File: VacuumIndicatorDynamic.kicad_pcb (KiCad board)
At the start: 2 copper layers, 96 parts, among them J1 Conn_01x02_Male, J2 Conn_01x03_Male, J3 Conn_01x03_Male, J4 Conn_01x03_Male, SW1 SW_DIP_x01, SW2 SW_DIP_x01, SW3 SW_DIP_x01, SW4 SW_DIP_x01, U1 AP1117-25, U2 YAAJ_BluePill

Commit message: update pcb
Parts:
- added REF**: KiCad-Logo2_8mm_Copper, Symbol:KiCad-Logo2_8mm_Copper, F.Cu at (85.7, 109.9)
- J1: moved to B.Cu
- moved R38 35.0 mm to (184.8, 34.3)
- moved R42 35.0 mm to (184.8, 40.4)
- moved R46 35.0 mm to (175.5, 36.2)
- moved VT22 35.0 mm to (179.8, 36.2)
- moved R50 35.0 mm to (175.9, 40.6)
- moved VT26 35.0 mm to (180.9, 39.4)
- moved R21 24.4 mm to (160.8, 117.0), turned to 180 degrees
- moved VT15 20.3 mm to (161.9, 113.7), turned to 180 degrees
- moved R31 20.2 mm to (160.0, 108.7), turned to 90 degrees
- moved R16 18.8 mm to (166.5, 117.0), turned to 180 degrees
- moved VT10 15.7 mm to (165.1, 112.5), turned to 0 degrees
- moved R26 13.2 mm to (165.1, 108.7), turned to 90 degrees
- moved R34 11.4 mm to (176.5, 90.8)
- moved VT24 11.4 mm to (181.4, 64.1)
- moved R18 11.4 mm to (184.9, 97.2)
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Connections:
- U2 pad 11: /AU3 -> /AU9
- U2 pad 12: /AU4 -> /AU8
- U2 pad 13: /AU5 -> /AU7
- U2 pad 15: /AU7 -> /AU5
- U2 pad 16: /AU8 -> /AU4
- U2 pad 17: /AU9 -> /AU3
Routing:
- net +2V5: track 215.3 -> 184.3 mm, vias 1 -> 2
- net /A3: track 19.1 -> 32.7 mm
- net /A6: track 31.2 -> 19.4 mm
- net /A7: track 38.4 -> 26.6 mm
- net +24V: track 234.6 -> 223.4 mm
- net /A2: track 28.5 -> 38.6 mm
- net /A4: track 14.0 -> 22.9 mm
- net GND: track 670.9 -> 662.2 mm, vias 11 -> 13
- net Net-(R38-Pad2): track 0.00 -> 8.06 mm
- net /A5: track 21.6 -> 14.2 mm
- net +3V3: track 123.7 -> 130.6 mm
- net /A1: track 36.3 -> 29.9 mm
- net Net-(R42-Pad2): track 0.00 -> 4.19 mm
- net /A8: track 30.0 -> 33.5 mm
- net +5V: track 245.0 -> 248.4 mm
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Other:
- board text added: "Dolgopolov"

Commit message: update pcb
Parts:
- moved J4 1.90 mm to (183.5, 28.6)
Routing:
- net GND: track 662.2 -> 695.5 mm
- net +24V: track 223.4 -> 228.7 mm
- net /A9: track 47.5 -> 50.5 mm
- net /AU8: track 44.5 -> 47.1 mm, vias 1 -> 2
- net /AU1: track 102.9 -> 100.4 mm
- net Net-(EL1-Pad12): track 144.2 -> 146.4 mm
- net /A7: track 26.6 -> 24.6 mm
- net Net-(EL1-Pad13): track 137.0 -> 139.0 mm
- net +2V5: track 184.3 -> 186.2 mm
- net /BTN1: track 97.5 -> 95.8 mm
- net /BTN2: track 83.3 -> 81.7 mm
- net Net-(EL1-Pad14): track 129.2 -> 130.8 mm
- net +3V3: track 130.6 -> 129.0 mm
- net /N: track 97.6 -> 96.2 mm
- net /AU2: track 100.1 -> 98.8 mm
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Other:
- board outline added: 167.2 x 100.6 mm

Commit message: pcb update. ready for fabrication
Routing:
- added copper zone on F.Cu, net GND
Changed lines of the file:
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@@
   (arc (start 41.783 57.277) (mid 41.783 57.277) (end 41.783 57.277) (width 0.4) (layer "F.Cu") (net 102))
   (segment (start 177.5575 99.06) (end 180.455 99.06) (width 0.8) (layer "F.Cu") (net 104))
+  (zone (net 2) (net_name "GND") (layer "F.Cu") (hatch edge 0.508)
+    (priority 1)
+    (connect_pads (clearance 1))
+    (min_thickness 0.254) (filled_areas_thickness no)
+    (fill yes (mode hatch) (thermal_gap 0.508) (thermal_bridge_width 0.508)
+      (hatch_thickness 1.016) (hatch_gap 1.524) (hatch_orientation 45)
+      (hatch_border_algorithm hatch_thickness) (hatch_min_hole_area 0.3))
+    (polygon
+      (pts
+        (xy 193 124)
+        (xy 123 124)
+        (xy 123 24)
+        (xy 193 24)
+      )
+    )
+  )
+  (zone (net 2) (net_name "GND") (layer "F.Cu") (hatch edge 0.508)
+    (priority 1)
+    (connect_pads (clearance 1))
+    (min_thickness 0.254) (filled_areas_thickness no)
+    (fill yes (mode hatch) (thermal_gap 0.508) (thermal_bridge_width 0.508)
+      (hatch_thickness 1.016) (hatch_gap 1.524) (hatch_orientation 45)
+      (hatch_border_algorithm hatch_thickness) (hatch_min_hole_area 0.3))
+    (polygon
+      (pts
+        (xy 96 124)
+        (xy 26 124)
+        (xy 26 23)
+        (xy 96 23)
+      )
+    )
+  )
 )

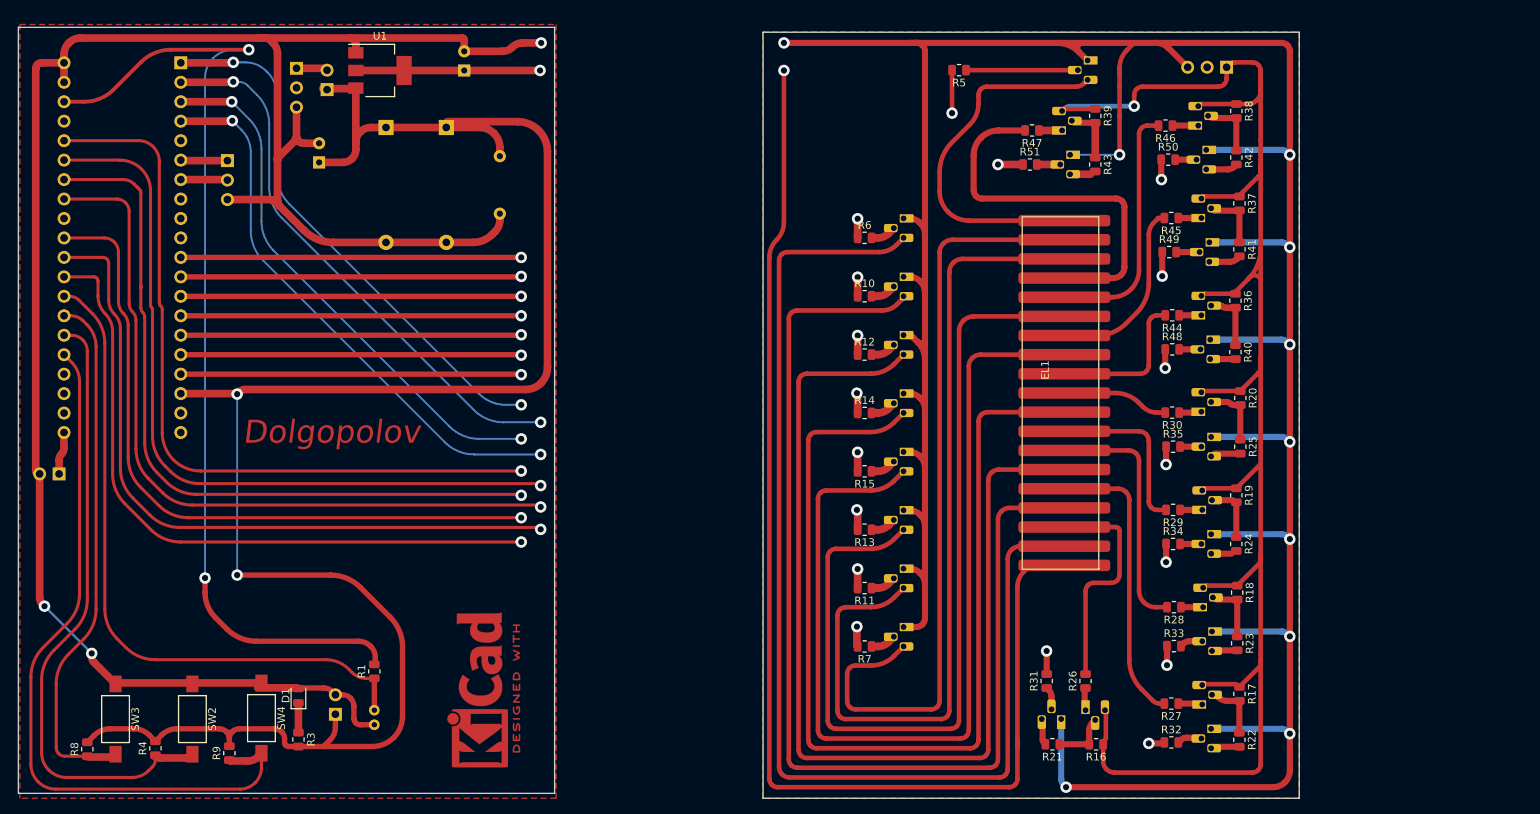
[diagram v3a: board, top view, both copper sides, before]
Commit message: remove copper area add mounting holes
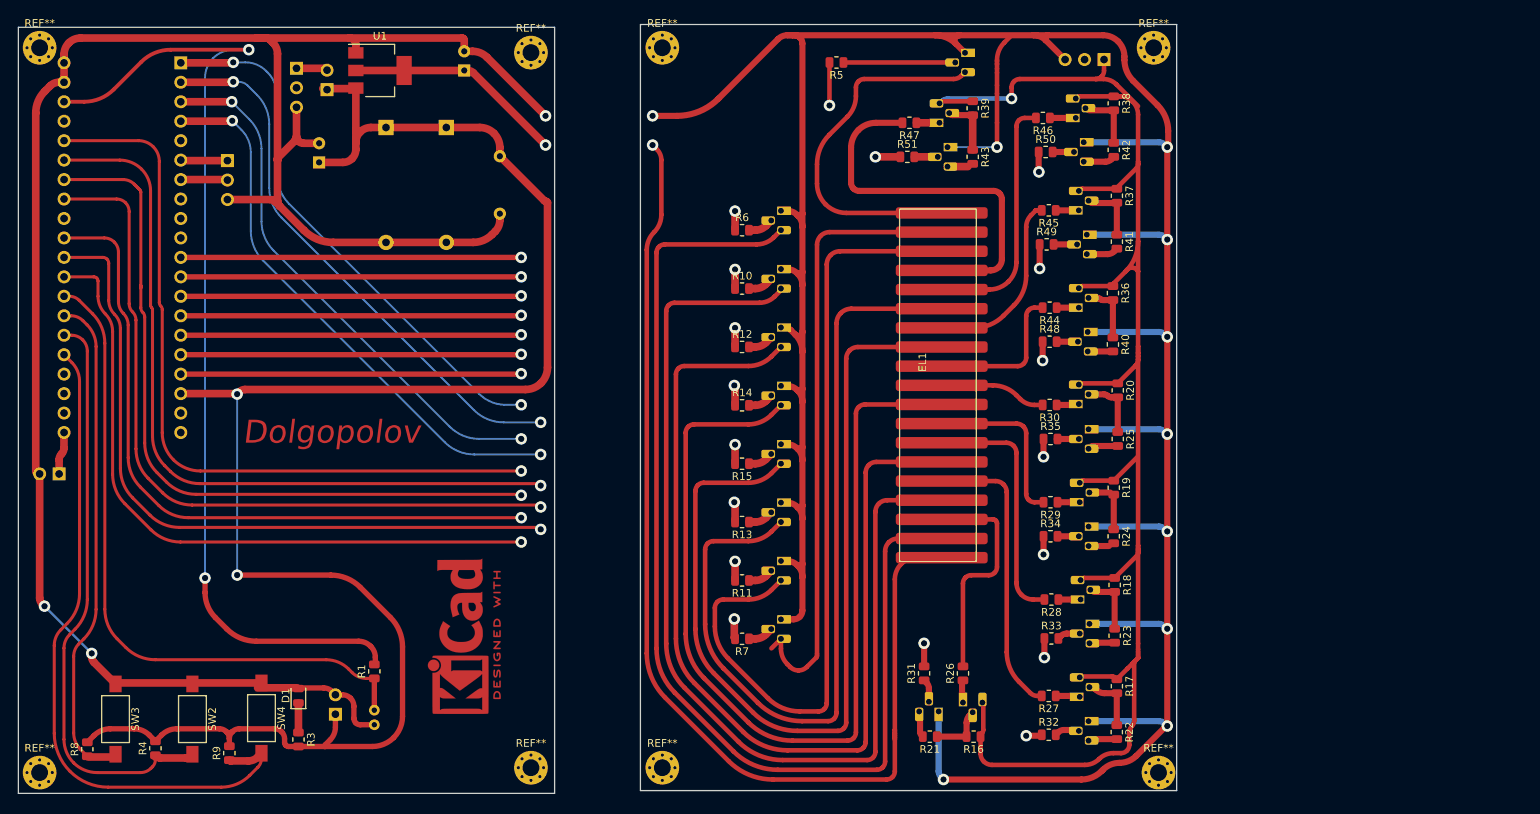
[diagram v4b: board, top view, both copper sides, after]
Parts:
- added REF**: MountingHole_2.2mm_M2_Pad_Via, MountingHole:MountingHole_2.2mm_M2_Pad_Via, F.Cu at (28.6, 26.0)
- added REF**: MountingHole_2.2mm_M2_Pad_Via, MountingHole:MountingHole_2.2mm_M2_Pad_Via, F.Cu at (174.6, 120.7)
- added REF**: MountingHole_2.2mm_M2_Pad_Via, MountingHole:MountingHole_2.2mm_M2_Pad_Via, F.Cu at (174.0, 26.0)
- added REF**: MountingHole_2.2mm_M2_Pad_Via, MountingHole:MountingHole_2.2mm_M2_Pad_Via, F.Cu at (109.9, 26.0)
- added REF**: MountingHole_2.2mm_M2_Pad_Via, MountingHole:MountingHole_2.2mm_M2_Pad_Via, F.Cu at (92.7, 120.0)
- added REF**: MountingHole_2.2mm_M2_Pad_Via, MountingHole:MountingHole_2.2mm_M2_Pad_Via, F.Cu at (109.9, 120.0)
- added REF**: MountingHole_2.2mm_M2_Pad_Via, MountingHole:MountingHole_2.2mm_M2_Pad_Via, F.Cu at (92.7, 26.7)
- added REF**: MountingHole_2.2mm_M2_Pad_Via, MountingHole:MountingHole_2.2mm_M2_Pad_Via, F.Cu at (28.6, 120.7)
- moved R10 16.0 mm to (120.3, 57.5)
- moved R11 16.0 mm to (120.3, 95.6)
- moved R12 16.0 mm to (120.3, 65.1)
- moved R13 16.0 mm to (120.3, 87.9)
- moved R14 16.0 mm to (120.3, 72.7)
- moved R15 16.0 mm to (120.3, 80.3)
- moved R6 16.0 mm to (120.3, 49.8)
- moved R7 16.0 mm to (120.3, 103.2)
- moved EL1 16.0 mm to (147.8, 70.1)
- moved J4 16.0 mm to (167.5, 27.6)
- moved R16 16.0 mm to (150.5, 116.0)
- moved R17 16.0 mm to (169.2, 109.4)
- moved R18 16.0 mm to (168.9, 96.2)
- moved R19 16.0 mm to (168.8, 83.5)
- moved R20 16.0 mm to (169.3, 70.8)
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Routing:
- net Net-(EL1-Pad19): track 101.4 -> 81.1 mm
- net +2V5: track 186.2 -> 172.8 mm
- net +5V: track 248.2 -> 235.0 mm
- net +24V: track 228.7 -> 219.4 mm
- net Net-(EL1-Pad12): track 146.4 -> 138.9 mm
- net Net-(EL1-Pad13): track 139.0 -> 131.8 mm
- net /BTN1: track 95.8 -> 88.9 mm
- net Net-(EL1-Pad14): track 130.8 -> 123.9 mm
- net Net-(EL1-Pad15): track 125.7 -> 119.2 mm
- net Net-(EL1-Pad16): track 124.5 -> 118.4 mm
- net Net-(EL1-Pad17): track 116.7 -> 110.9 mm
- net Net-(EL1-Pad18): track 112.1 -> 106.9 mm
- net /BTN2: track 81.7 -> 77.0 mm
- net /BTN3: track 68.9 -> 65.1 mm
- net GND: track 695.5 -> 692.5 mm
- removed copper zone on F.Cu, net GND
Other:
- board size 167.2 x 100.6 mm -> 151.2 x 100.4 mm

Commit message: several pcb updates
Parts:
- removed the REF** at (92.7, 120.0)
- removed the REF** at (109.9, 120.0)
- added REF**: MountingHole_2.2mm_M2_Pad_Via, MountingHole:MountingHole_2.2mm_M2_Pad_Via, F.Cu at (92.7, 120.7)
- added REF**: MountingHole_2.2mm_M2_Pad_Via, MountingHole:MountingHole_2.2mm_M2_Pad_Via, F.Cu at (109.9, 120.7)
- C3: footprint Capacitor_THT:C_Axial_L5.1mm_D3.1mm_P7.50mm_Horizontal -> Capacitor_SMD:C_0805_2012Metric; moved to F.Cu
- C4: footprint Capacitor_THT:CP_Axial_L10.0mm_D6.0mm_P15.00mm_Horizontal -> Capacitor_SMD:C_0805_2012Metric; moved to F.Cu
- C5: footprint Capacitor_THT:CP_Axial_L10.0mm_D6.0mm_P15.00mm_Horizontal -> Capacitor_THT:CP_Radial_D8.0mm_P5.00mm
- moved C3 6.51 mm to (92.1, 45.7)
- moved C1 6.48 mm to (68.6, 35.6), turned to -90 degrees
- moved REF** 5.12 mm to (85.7, 107.3)
- moved C4 2.62 mm to (76.2, 37.5)
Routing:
- net +5V: track 235.0 -> 228.6 mm
- net GND: track 692.5 -> 688.1 mm
- added copper zone on F.Cu, net GND

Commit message: major pcb update
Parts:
- added R52: 510, Resistor_SMD:R_0805_2012Metric, F.Cu at (138.1, 68.6)
- added R53: 510, Resistor_SMD:R_0805_2012Metric, F.Cu at (138.2, 74.9)
- added R54: 510, Resistor_SMD:R_0805_2012Metric, F.Cu at (138.2, 80.5)
- added R55: 510, Resistor_SMD:R_0805_2012Metric, F.Cu at (138.2, 88.6)
- added R56: 4.7k, Resistor_SMD:R_0805_2012Metric, F.Cu at (117.3, 67.8)
- added R57: 4.7k, Resistor_SMD:R_0805_2012Metric, F.Cu at (117.3, 74.4)
- added R58: 4.7k, Resistor_SMD:R_0805_2012Metric, F.Cu at (117.3, 80.8)
- added R59: 4.7k, Resistor_SMD:R_0805_2012Metric, F.Cu at (117.3, 87.6)
- R10, R14, R15, R16, R20, R31, R32, R33, R48, R49, R50, R51: value 4.7k -> 47k
- R22, R23, R24, R25, R40, R41, R42, R43: value 47k -> 4.7k
- R26, R27, R28, R44, R45, R46, R47: value 510 -> 4.7k
- R29, R30: value 510 -> 47k
- R34, R35, R36, R37, R38: value 4.7k -> 510
- R6, R7: value 4.7k -> 10k
- R8, R9: value 10k -> 47k
- moved R8 139.4 mm to (154.9, 46.8), turned to 0 degrees
- moved R6 108.9 mm to (34.9, 117.5), turned to 90 degrees
- moved R9 105.8 mm to (154.4, 87.0), turned to 0 degrees
- moved VT16 86.9 mm to (122.7, 38.3)
- moved VT15 84.3 mm to (122.7, 31.6), turned to -90 degrees
- moved VT10 79.8 mm to (134.2, 33.1), turned to 180 degrees
- moved VT11 77.0 mm to (134.4, 39.8), turned to 180 degrees
- moved VT17 70.6 mm to (122.7, 45.2)
- moved R32 70.4 mm to (126.2, 54.1), turned to -90 degrees
- moved R24 69.3 mm to (128.6, 33.4), turned to 90 degrees
- moved R7 68.5 mm to (53.3, 117.8), turned to 90 degrees
- moved R27 64.6 mm to (129.0, 54.1), turned to 90 degrees
- moved R26 64.3 mm to (129.3, 46.5)
- moved VT5 63.9 mm to (174.8, 52.4), turned to 180 degrees
- moved R31 63.8 mm to (126.2, 46.5), turned to -90 degrees
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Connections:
- EL1 pad 1: +2V5 -> Net-(EL1-Pad1)
- EL1 pad 12: Net-(EL1-Pad12) -> /S_OUT_1
- EL1 pad 13: Net-(EL1-Pad13) -> /S_OUT_2
- EL1 pad 14: Net-(EL1-Pad14) -> /S_OUT_3
- EL1 pad 15: Net-(EL1-Pad15) -> /S_OUT_4
- EL1 pad 16: Net-(EL1-Pad16) -> /S_OUT_5
- EL1 pad 17: Net-(EL1-Pad17) -> /S_OUT_6
- EL1 pad 18: Net-(EL1-Pad18) -> /S_OUT_7
- EL1 pad 19: Net-(EL1-Pad19) -> /S_OUT_8
- EL1 pad 2: Net-(EL1-Pad2) -> +2V5
- R10 pad 1: /K2 -> +24V
- R10 pad 2: Net-(R10-Pad2) -> /S_OUT_7
- R11 pad 1: Net-(R11-Pad1) -> /S1
- R11 pad 2: /K7 -> Net-(R11-Pad2)
- R12 pad 1: /K3 -> Net-(R12-Pad1)
- R12 pad 2: Net-(R12-Pad2) -> /S8
- R13 pad 2: /K6 -> /S7
- R14 pad 1: /K4 -> +24V
- R14 pad 2: Net-(R14-Pad2) -> /S_OUT_2
- R15 pad 1: Net-(R15-Pad1) -> +24V
- R15 pad 2: /K5 -> /S_OUT_3
- R16 pad 2: Net-(R16-Pad2) -> /S_OUT_6
- R17 pad 1: +24V -> /S2
- R18 pad 1: +24V -> /S3
- R19 pad 1: +24V -> Net-(R19-Pad1)
- R19 pad 2: Net-(R19-Pad2) -> /S6
- R20 pad 2: Net-(R20-Pad2) -> /S_OUT_4
- R21 pad 1: Net-(R16-Pad2) -> +24V
- R21 pad 2: Net-(R21-Pad2) -> /S_OUT_5
- R22 pad 1: Net-(R17-Pad2) -> /S4
- R23 pad 1: Net-(R18-Pad2) -> Net-(R23-Pad1)
- R23 pad 2: Net-(R23-Pad2) -> /S5
- R24 pad 1: Net-(R19-Pad2) -> +24V
- R25 pad 1: Net-(R20-Pad2) -> +24V
- R26 pad 1: Net-(R26-Pad1) -> +24V
- R26 pad 2: /A1 -> Net-(R26-Pad2)
- R27 pad 1: Net-(R27-Pad1) -> +24V
- R27 pad 2: /A2 -> Net-(R27-Pad2)
- R28 pad 1: Net-(R28-Pad1) -> +24V
- R28 pad 2: /A3 -> Net-(R28-Pad2)
- R29 pad 1: Net-(R29-Pad1) -> Net-(R24-Pad2)
- R29 pad 2: /A4 -> Net-(R29-Pad2)
- R30 pad 1: Net-(R30-Pad1) -> Net-(R25-Pad2)
- R30 pad 2: /A5 -> Net-(R30-Pad2)
- R31 pad 1: Net-(R31-Pad1) -> Net-(R26-Pad2)
- R31 pad 2: /AU1 -> Net-(R31-Pad2)
- R32 pad 1: /AU2 -> Net-(R27-Pad2)
- R33 pad 1: /AU3 -> Net-(R28-Pad2)
- R34 pad 1: /AU4 -> Net-(R34-Pad1)
- R34 pad 2: Net-(R34-Pad2) -> /A1
- R35 pad 1: /AU5 -> Net-(R35-Pad1)
- R35 pad 2: Net-(R35-Pad2) -> /A2
- R36 pad 1: +24V -> Net-(R36-Pad1)
- R36 pad 2: Net-(R36-Pad2) -> /A3
- R37 pad 1: +24V -> Net-(R37-Pad1)
- R37 pad 2: Net-(R37-Pad2) -> /A4
- R38 pad 1: +24V -> Net-(R38-Pad1)
- R38 pad 2: Net-(R38-Pad2) -> /A5
- R39 pad 1: +24V -> Net-(R39-Pad1)
- R39 pad 2: Net-(R39-Pad2) -> /AU1
- R40 pad 1: Net-(R36-Pad2) -> /AU2
- R41 pad 1: Net-(R37-Pad2) -> /AU3
- R42 pad 1: Net-(R38-Pad2) -> /AU4
- R43 pad 1: Net-(R39-Pad2) -> /AU5
- R44 pad 1: Net-(R44-Pad1) -> +24V
- R44 pad 2: /A6 -> Net-(R44-Pad2)
- R45 pad 1: Net-(R45-Pad1) -> +24V
- R45 pad 2: /A7 -> Net-(R45-Pad2)
- R46 pad 1: Net-(R46-Pad1) -> +24V
- R46 pad 2: /A8 -> Net-(R46-Pad2)
- R47 pad 1: Net-(R47-Pad1) -> +24V
- R47 pad 2: /A9 -> Net-(R47-Pad2)
- R48 pad 1: /AU6 -> Net-(R44-Pad2)
- R49 pad 1: /AU7 -> Net-(R45-Pad2)
- R50 pad 1: /AU8 -> Net-(R46-Pad2)
- R51 pad 1: /AU9 -> Net-(R47-Pad2)
- R6 pad 1: /K1 -> /BTN3
- R6 pad 2: Net-(R6-Pad2) -> +5V
- R7 pad 1: Net-(R7-Pad1) -> /BTN1
- R7 pad 2: /K8 -> +5V
- R8 pad 1: /BTN3 -> +24V
- R8 pad 2: +5V -> /S_OUT_1
- R9 pad 1: /BTN1 -> +24V
- R9 pad 2: +5V -> /S_OUT_8
- U2 pad 1: /K3 -> /S3
- U2 pad 11: /AU9 -> /AU1
- U2 pad 12: /AU8 -> /AU2
- U2 pad 13: /AU7 -> /AU3
- U2 pad 14: /AU6 -> /AU4
- U2 pad 16: /AU4 -> /AU6
- U2 pad 17: /AU3 -> /AU7
- U2 pad 2: /K4 -> /S4
- U2 pad 29: /K8 -> /S8
- U2 pad 3: /K5 -> /S5
- U2 pad 30: /K7 -> /S7
- U2 pad 33: /AU1 -> /AU9
- U2 pad 34: /AU2 -> /AU8
- U2 pad 35: /K1 -> /S1
- U2 pad 36: /K2 -> /S2
- U2 pad 4: /K6 -> /S6
- VT1 pad 3: Net-(EL1-Pad2) -> Net-(EL1-Pad1)
- VT10 pad 1: Net-(R26-Pad1) -> Net-(R34-Pad1)
- VT10 pad 2: Net-(R16-Pad2) -> Net-(R24-Pad2)
- VT11 pad 1: Net-(R27-Pad1) -> Net-(R35-Pad1)
- VT11 pad 2: Net-(R17-Pad2) -> Net-(R25-Pad2)
- VT12 pad 1: Net-(R28-Pad1) -> Net-(R36-Pad1)
- VT12 pad 2: Net-(R18-Pad2) -> Net-(R26-Pad2)
- VT13 pad 1: Net-(R29-Pad1) -> Net-(R37-Pad1)
- VT13 pad 2: Net-(R19-Pad2) -> Net-(R27-Pad2)
- VT14 pad 1: Net-(R30-Pad1) -> Net-(R38-Pad1)
- VT14 pad 2: Net-(R20-Pad2) -> Net-(R28-Pad2)
- VT15 pad 2: Net-(R31-Pad1) -> Net-(R39-Pad1)
- VT15 pad 3: Net-(R21-Pad2) -> Net-(R29-Pad2)
- VT16 pad 2: Net-(R32-Pad2) -> Net-(R40-Pad2)
- VT16 pad 3: Net-(R22-Pad2) -> Net-(R30-Pad2)
- VT17 pad 2: Net-(R33-Pad2) -> Net-(R41-Pad2)
- VT17 pad 3: Net-(R23-Pad2) -> Net-(R31-Pad2)
- VT18 pad 2: Net-(R34-Pad2) -> Net-(R42-Pad2)
- VT18 pad 3: Net-(R24-Pad2) -> Net-(R32-Pad2)
- VT19 pad 2: Net-(R35-Pad2) -> Net-(R43-Pad2)
- VT19 pad 3: Net-(R25-Pad2) -> Net-(R33-Pad2)
- VT2 pad 2: Net-(R6-Pad2) -> Net-(R11-Pad2)
- VT2 pad 3: Net-(EL1-Pad12) -> /S_OUT_1
- VT20 pad 1: Net-(R44-Pad1) -> Net-(R52-Pad1)
- VT20 pad 2: Net-(R36-Pad2) -> Net-(R44-Pad2)
- VT21 pad 1: Net-(R45-Pad1) -> Net-(R53-Pad1)
- VT21 pad 2: Net-(R37-Pad2) -> Net-(R45-Pad2)
- VT22 pad 1: Net-(R46-Pad1) -> Net-(R54-Pad1)
- VT22 pad 2: Net-(R38-Pad2) -> Net-(R46-Pad2)
- VT23 pad 1: Net-(R47-Pad1) -> Net-(R55-Pad1)
- VT23 pad 2: Net-(R39-Pad2) -> Net-(R47-Pad2)
- VT24 pad 2: Net-(R48-Pad2) -> Net-(R56-Pad2)
- VT24 pad 3: Net-(R40-Pad2) -> Net-(R48-Pad2)
- VT25 pad 2: Net-(R49-Pad2) -> Net-(R57-Pad2)
- VT25 pad 3: Net-(R41-Pad2) -> Net-(R49-Pad2)
- VT26 pad 2: Net-(R50-Pad2) -> Net-(R58-Pad2)
- VT26 pad 3: Net-(R42-Pad2) -> Net-(R50-Pad2)
- VT27 pad 2: Net-(R51-Pad2) -> Net-(R59-Pad2)
- VT27 pad 3: Net-(R43-Pad2) -> Net-(R51-Pad2)
- VT3 pad 2: Net-(R7-Pad1) -> Net-(R12-Pad1)
- VT3 pad 3: Net-(EL1-Pad19) -> /S_OUT_8
- VT4 pad 2: Net-(R10-Pad2) -> Net-(R13-Pad1)
- VT4 pad 3: Net-(EL1-Pad13) -> /S_OUT_7
- VT5 pad 2: Net-(R11-Pad1) -> Net-(R17-Pad2)
- VT5 pad 3: Net-(EL1-Pad18) -> /S_OUT_2
- VT6 pad 2: Net-(R12-Pad2) -> Net-(R18-Pad2)
- VT6 pad 3: Net-(EL1-Pad14) -> /S_OUT_3
- VT7 pad 2: Net-(R13-Pad1) -> Net-(R19-Pad1)
- VT7 pad 3: Net-(EL1-Pad17) -> /S_OUT_6
- VT8 pad 2: Net-(R14-Pad2) -> Net-(R22-Pad2)
- VT8 pad 3: Net-(EL1-Pad15) -> /S_OUT_4
- VT9 pad 2: Net-(R15-Pad1) -> Net-(R23-Pad1)
- VT9 pad 3: Net-(EL1-Pad16) -> /S_OUT_5
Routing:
- net Net-(EL1-Pad12): track 138.9 -> 0.00 mm
- net Net-(EL1-Pad13): track 131.8 -> 0.00 mm
- net Net-(EL1-Pad14): track 123.9 -> 0.00 mm
- net Net-(EL1-Pad15): track 119.2 -> 0.00 mm
- net Net-(EL1-Pad16): track 118.4 -> 0.00 mm
- net Net-(EL1-Pad17): track 110.9 -> 0.00 mm
- net Net-(EL1-Pad18): track 106.9 -> 0.00 mm
- net /K1: track 102.2 -> 0.00 mm, vias 2 -> 0
- net /S1: track 0.00 -> 102.0 mm, vias 0 -> 2
- net /K2: track 101.6 -> 0.00 mm, vias 2 -> 0
- net /S2: track 0.00 -> 101.4 mm, vias 0 -> 2
- net GND: track 688.1 -> 591.5 mm, vias 13 -> 4
- net Net-(R11-Pad2): track 0.00 -> 96.6 mm, vias 0 -> 2
- net /K7: track 94.8 -> 0.00 mm, vias 2 -> 0
- net /S7: track 0.00 -> 94.6 mm, vias 0 -> 2
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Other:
- board size 151.2 x 100.4 mm -> 151.2 x 100 mm
